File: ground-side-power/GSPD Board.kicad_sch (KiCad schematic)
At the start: 40 parts

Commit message: Addressed a few comments and added notes to schematic
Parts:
- removed C? (x6): 10uF, symbol Device:C_Small
- removed C? (x2): 100uF, symbol Device:C_Small
- removed C?: 0.33uF, symbol Device:C_Small
- removed C?: 0.1uF, symbol Device:C_Small
- removed U?: L7824CD2T, Package_TO_SOT_SMD:TO-252-3_TabPin2, symbol Regulator_Linear:IFX27001TFV15
- removed U? (x2): LM1085IT-12, symbol GSP:LM1085IT-12
- removed U?: VRB1205YMD-15WR3, symbol GSP:VRB1205YMD-15WR3
- removed U?: LD1085V50, symbol GSP:LD1085V50
- added C?: 10uF, symbol Device:C_Small
- added C?: 22uF, symbol Device:C_Small
- added U?: K7805-3AR3, Package_TO_SOT_SMD:TO-252-2, symbol Regulator_Linear:LF18_TO252
- U?: value URB2424LD-30WR3 -> URB2424LD-20WR3
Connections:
- net 12V Regulated is gone; now on net 12V Unregulated: F?.1
- net 24V Regulated is gone; now on net 24V Unregulated: F?.1
- net +BATT: now also C?.1, U?.1 (VI)
- net GND: now also C?.2, U?.2 (GND)
- net 24V Unregulated: now reaches C?.1, U?.4 (Vout)
- net 12V Unregulated: now reaches J?.1 (Pin_1)
- net 5V Regulated renamed 5V Unregulated
- net 5V Unregulated: now also C?.1, U?.3 (VO)
- no-connect marks 4 -> 2
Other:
- note added: "12A max"
- note added: "144 W max"
- note added: "2A"
- note added: "6A max"
- note added: "72 W max"
- note added: "8 awg wire required"
- note added: "K7805-3AR3. Non Isolated 7 dollars, high efficiency 15W"
- note added: "Total Power: 250 W max"
- note removed: "1 A"
- note removed: "12 W"
- note removed: "2 A"
- note removed: "2.5 W"
- note removed: "6A (max)"
- note removed: "72 W (max)"
- note removed: "Tantalum"
- note removed: "Total Power: 120.5 W (max)"
- moved on the sheet: J?, MES?

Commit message: Adressed common concerns
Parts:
- removed J?: Battery Terminals, symbol Connector:Screw_Terminal_01x02
- removed J?: To COM-18732, symbol Connector:Screw_Terminal_01x02
- removed J?: From COM-18732, symbol Connector:Screw_Terminal_01x02
- added J? (x5): Battery Terminals, symbol Connector:Screw_Terminal_01x02
- added J?: AC/DC Input, symbol Connector:Screw_Terminal_01x02
- added SW?: SW_SPDT, symbol Switch:SW_SPDT
- C?: value ?F -> 120uF
- F?: value 8A Fuse -> 13A Fuse
- F?: value 12A Fuse -> 23A Fuse
- ICL?: value SL12 1R010 -> SL32 2R025
- SW?: value 10A -> 23A
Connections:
- net 12V Unregulated is gone; now on net +BATT: F?.1
- net GND: now also C?.2, C?.2, C?.2, U?.2 (GND), U?.5 (0V), J?.1 (Pin_1), J?.1 (Pin_1), J?.1 (Pin_1), J?.1 (Pin_1), J?.1 (Pin_1), J?.2 (Pin_2)
- net PowerInput: now reaches F?.1
- net PowerInput: now also SW?.2 (B)
- new net: J?.2 (Pin_2), J?.2 (Pin_2), J?.2 (Pin_2), SW?.1 (A)
- new net: J?.1 (Pin_1), J?.2 (Pin_2), J?.2 (Pin_2), SW?.3 (C)
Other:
- note added: "10.5V - 13.5V"
- note added: "9V - 14V"
- note added: "Converters"
- note added: "Does RLCS have bulk capacitors on board? Or should there be one here to prevent voltage drop during peak power draw?"
- note added: "Source Selection"
- note removed: "Converters + LDO"
- note removed: "Debating whether this needs a cap here, since battery voltage should be extremly stable"
- moved on the sheet: C?, D?, F?, ICL?, MES?, R?, SW?, U?

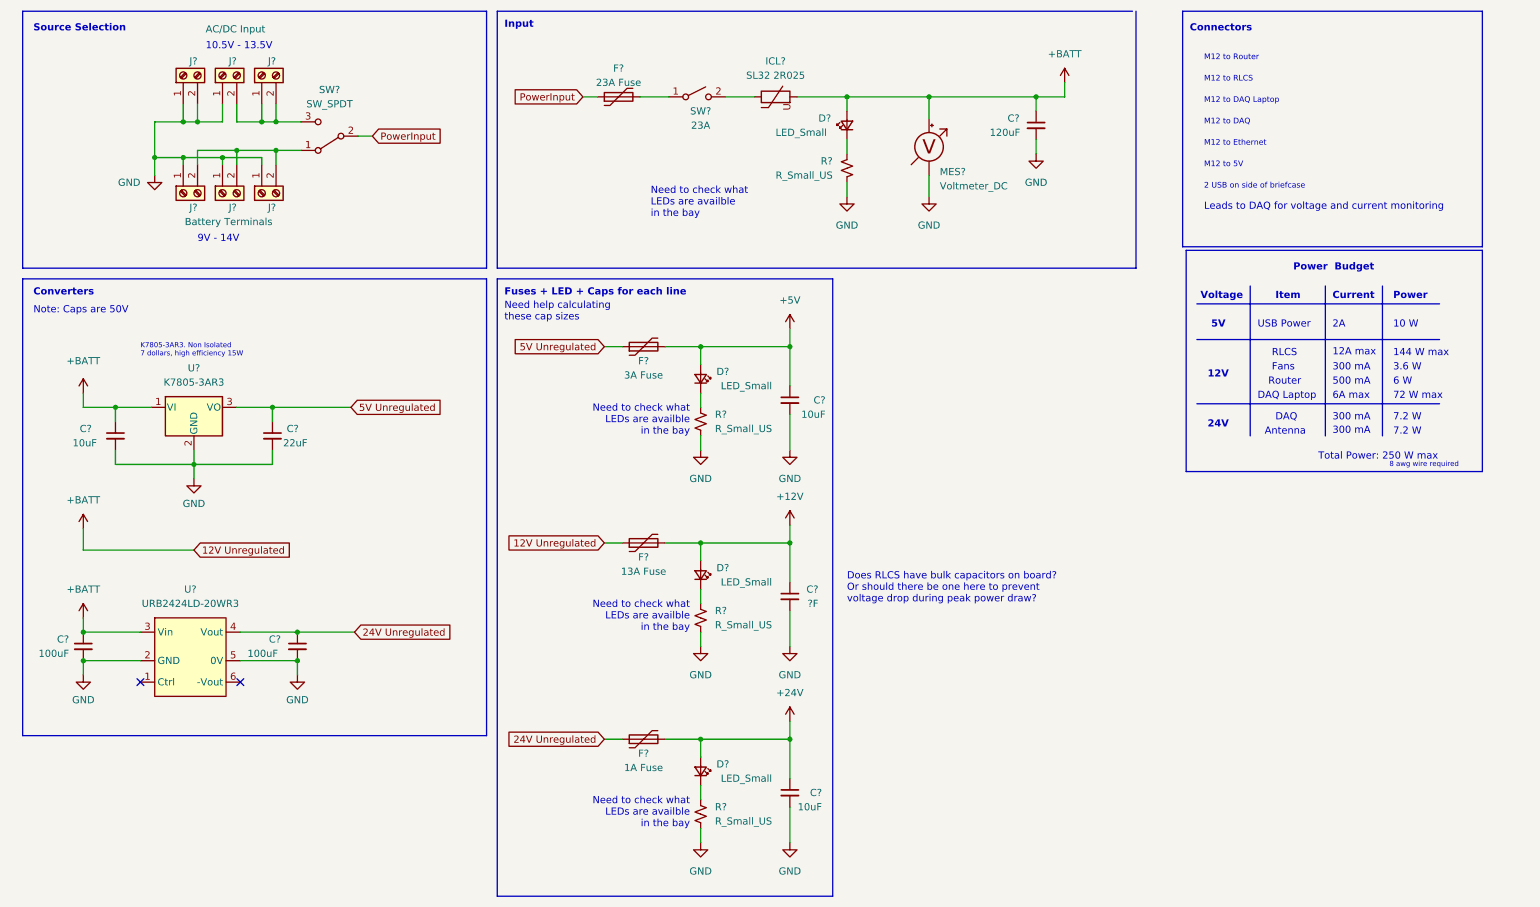
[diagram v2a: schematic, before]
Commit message: Added refrence designators
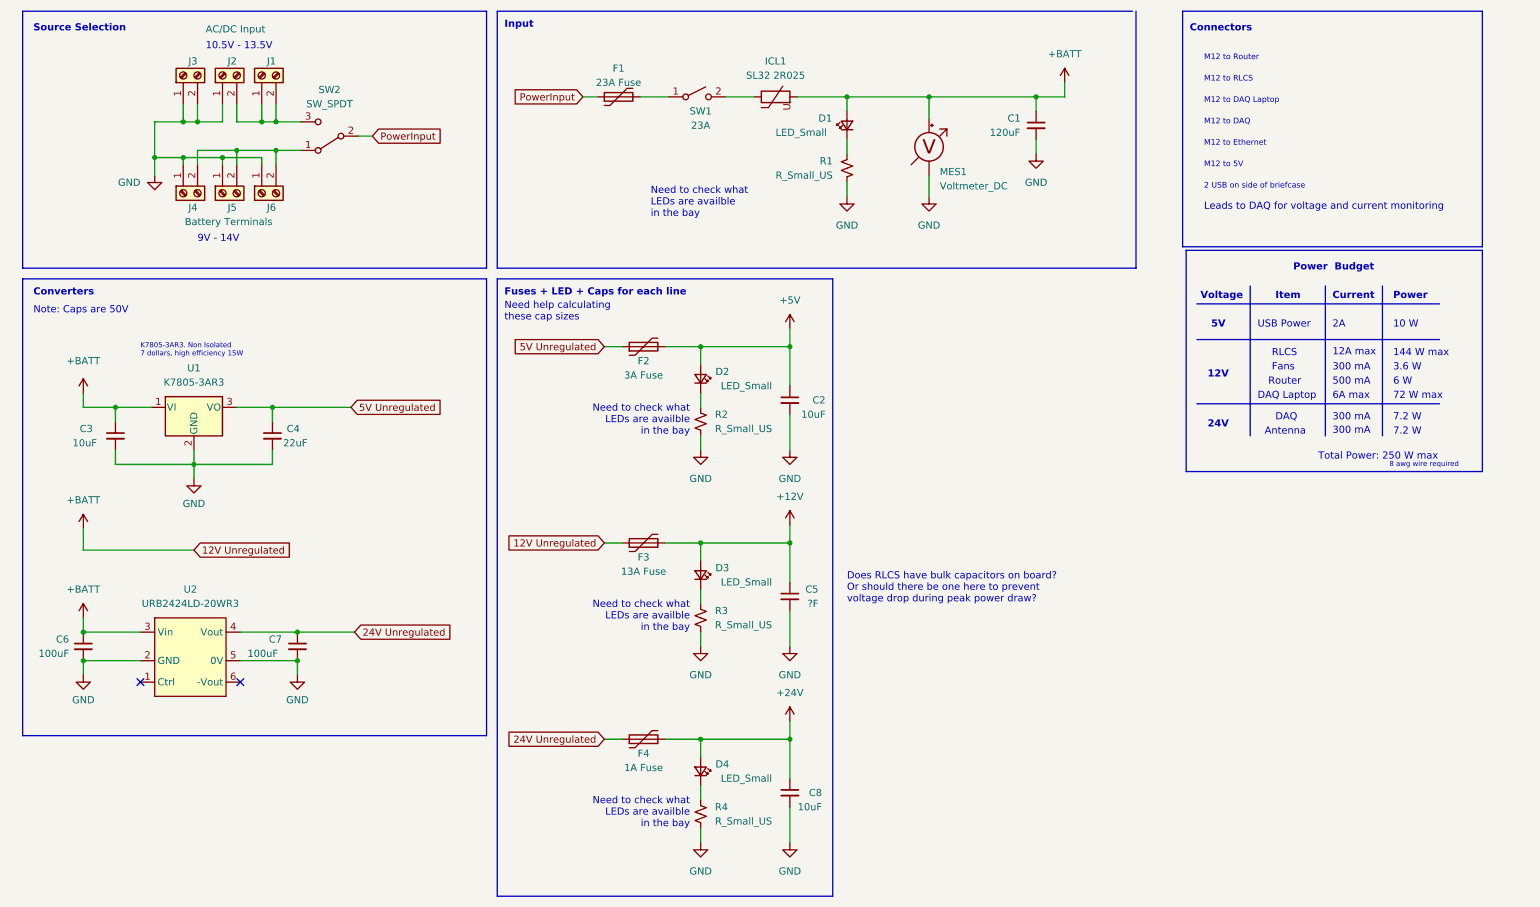
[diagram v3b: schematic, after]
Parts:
- gave numbers to parts that had none: 32

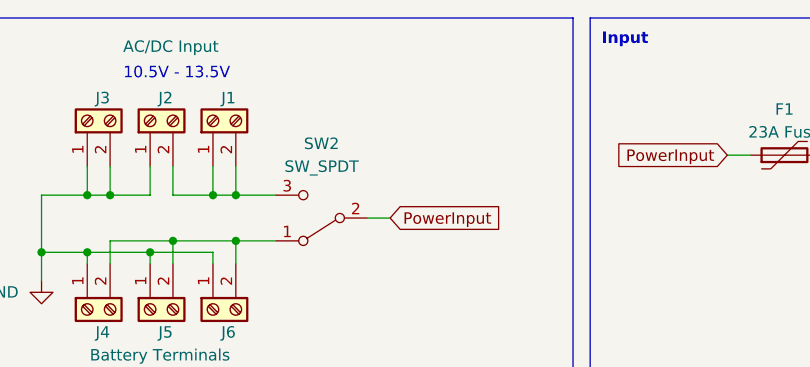
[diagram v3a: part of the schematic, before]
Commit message: Added Datasheets
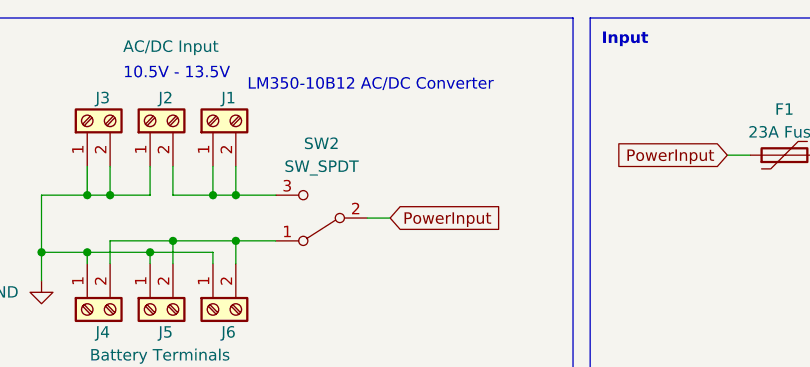
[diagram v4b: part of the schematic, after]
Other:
- note added: "LM350-10B12 AC/DC Converter"
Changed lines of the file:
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@@
     (effects (font (size 1 1)) (justify left bottom))
+  )
+  (text "LM350-10B12 AC/DC Converter" (at 64.135 26.035 0)
+    (effects (font (size 1.27 1.27)) (justify left bottom))
   )
   (text "Need to check what \nLEDs are availble\nin the bay" (at 136.525 93.345 180)

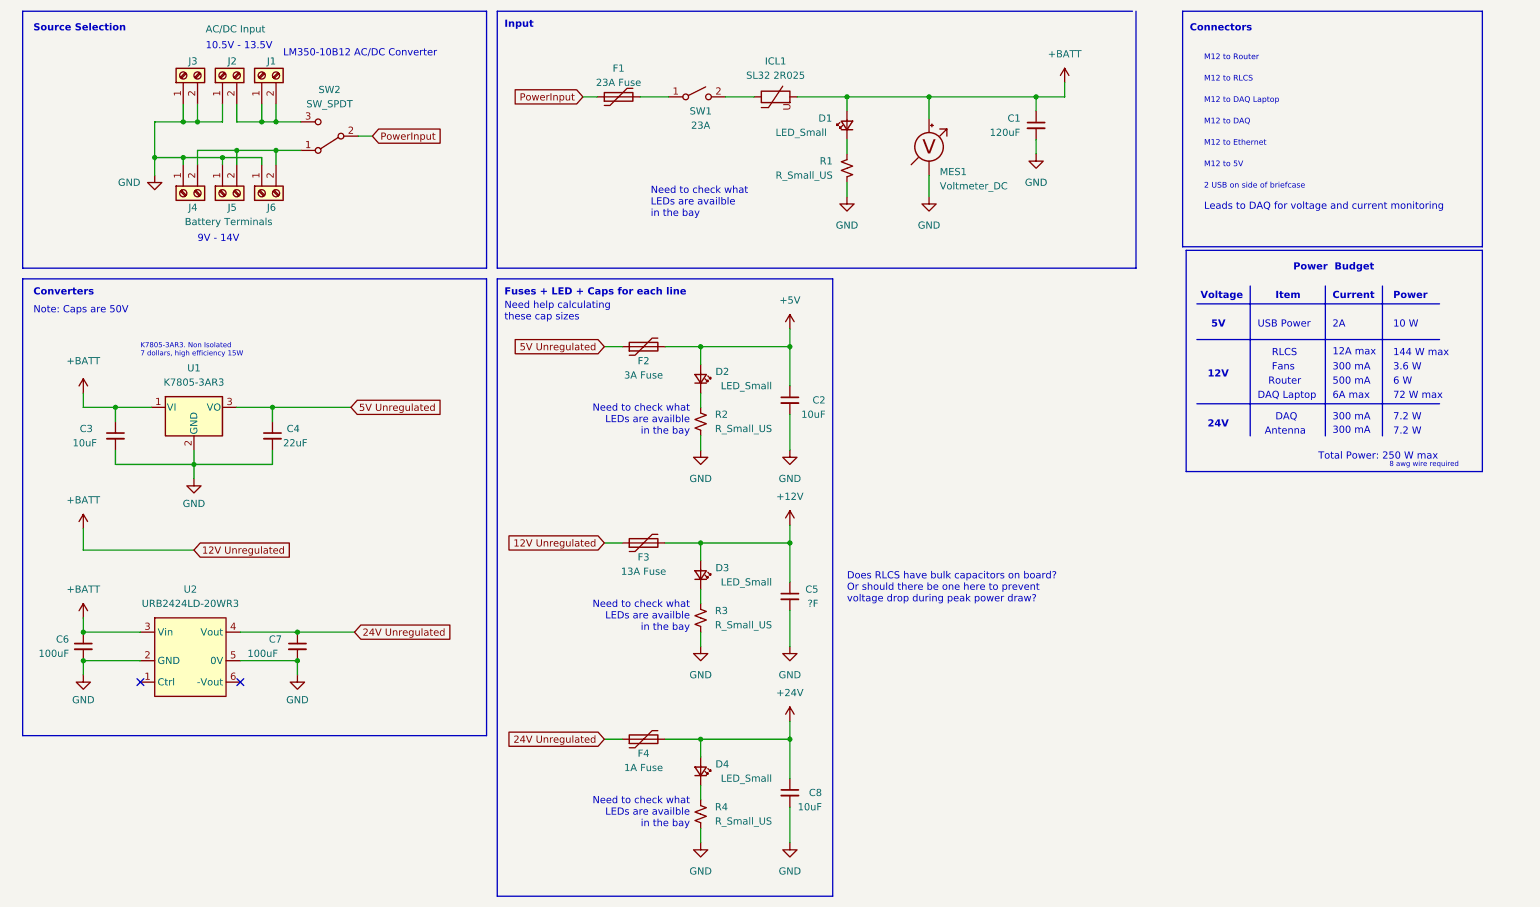
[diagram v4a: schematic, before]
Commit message: Polarity Protection
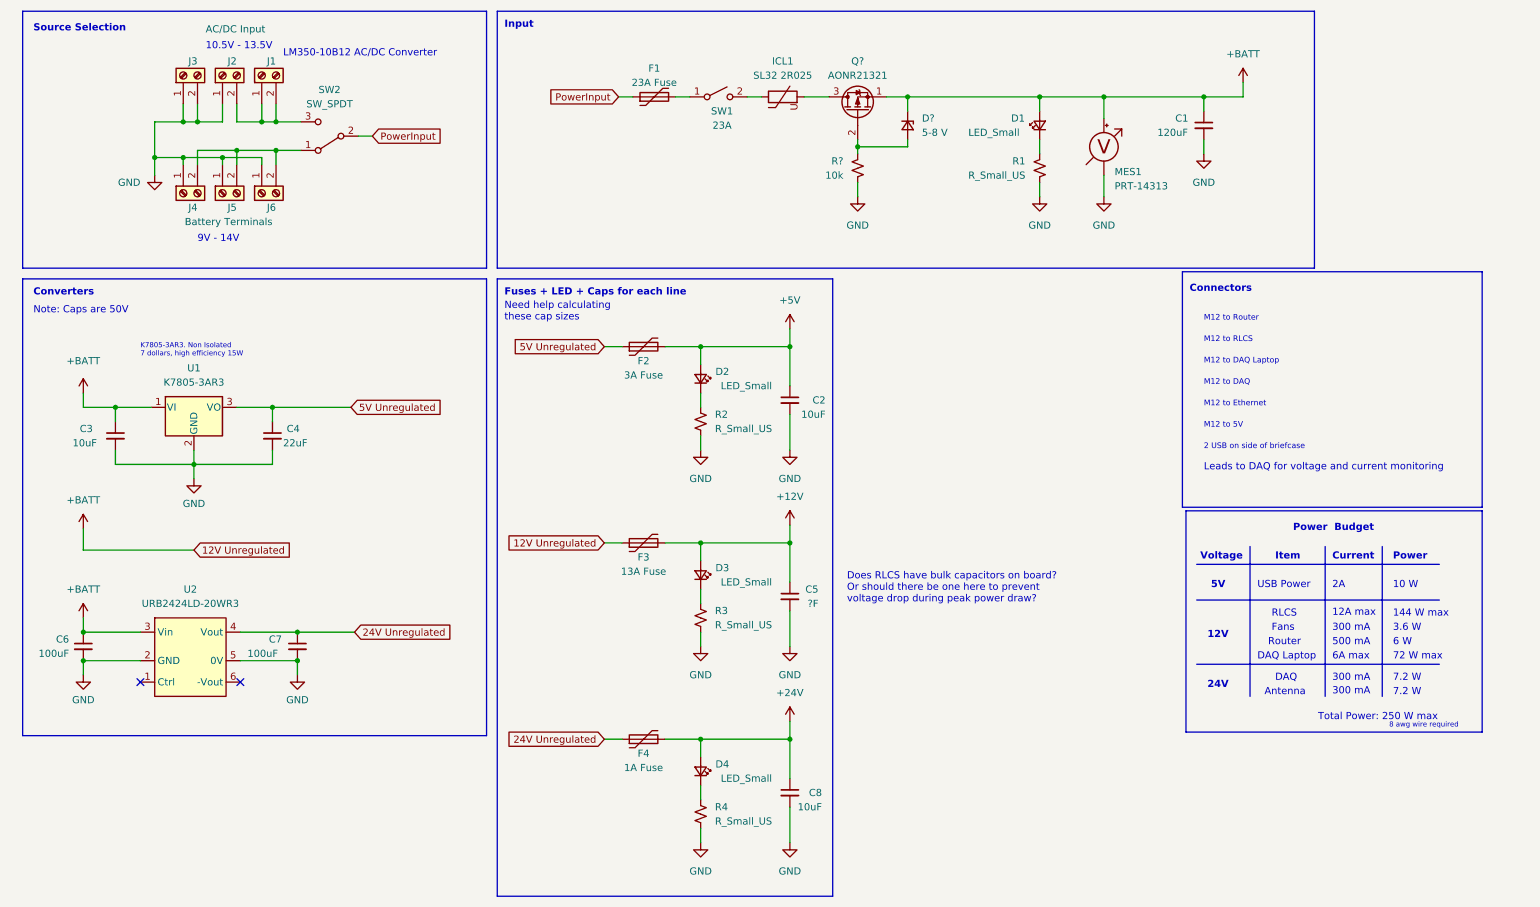
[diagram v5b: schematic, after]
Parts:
- added D?: 5-8 V, symbol Device:D_Zener_Small
- added Q?: AONR21321, symbol Device:Q_PMOS_SGD
- added R?: 10k, symbol Device:R_Small_US
- MES1: value Voltmeter_DC -> PRT-14313
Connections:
- net +BATT: now also D?.1 (K), Q?.1 (S); no longer ICL1.2
- net GND: now also R?.1
- new net: D?.2 (A), Q?.2 (G), R?.2
- new net: ICL1.2, Q?.3 (D)
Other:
- note removed: "Need to check what LEDs are availble in the bay"
- moved on the sheet: C1, D1, F1, ICL1, MES1, R1, SW1

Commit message: Addressed some comments, will continue working on it tomorrow
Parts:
- removed D?: 5-8 V, symbol Device:D_Zener_Small
- removed J1: Battery Terminals, symbol Connector:Screw_Terminal_01x02
- removed J3: AC/DC Input, symbol Connector:Screw_Terminal_01x02
- removed Q?: AONR21321, symbol Device:Q_PMOS_SGD
- removed R?: 10k, symbol Device:R_Small_US
- removed U1: K7805-3AR3, Package_TO_SOT_SMD:TO-252-2, symbol Regulator_Linear:LF18_TO252
- added D? (x2): DIODE, symbol Simulation_SPICE:DIODE
- added J?: Battery Terminals, symbol Connector:Screw_Terminal_01x02
- added U?: K7805-3AR3, Package_TO_SOT_SMD:TSOT-23-6, symbol Regulator_Switching:AP63203WU
- added U?: relay, symbol custom:relay
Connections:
- net +BATT: now also U?.3 (VIN), U?.7 (Swout)
- net 5V Unregulated: now also U?.5 (+VO1)
- net GND: now also D?.1 (A), J?.1 (Pin_1), U?.4 (GND), U?.6 (Cout)
- net at J4.2 (Pin_2), J5.2 (Pin_2), J6.2 (Pin_2)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: now also J?.2 (Pin_2)
- net at ICL1.2: now also D?.1 (A), U?.1 (Swin)
- new net: D?.2 (K), D?.2 (K), U?.2 (Cin)
- no-connect marks 2 -> 5
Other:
- note added: "12V (37.5A)"
- note added: "14 awg wire required"
- note added: "AGV650 PC Power Supply"
- note removed: "10.5V - 13.5V"
- note removed: "8 awg wire required"
- note removed: "K7805-3AR3. Non Isolated 7 dollars, high efficiency 15W"
- note removed: "LM350-10B12 AC/DC Converter"
- moved on the sheet: C1, C3, C4, D1, F1, ICL1, J2, J4, J5, J6, MES1, R1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
